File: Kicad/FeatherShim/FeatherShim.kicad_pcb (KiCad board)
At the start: 2 copper layers, 51 x 33 mm, 3 parts, among them P1 Feather, P2 CONN_01X16, P3 CONN_01X12

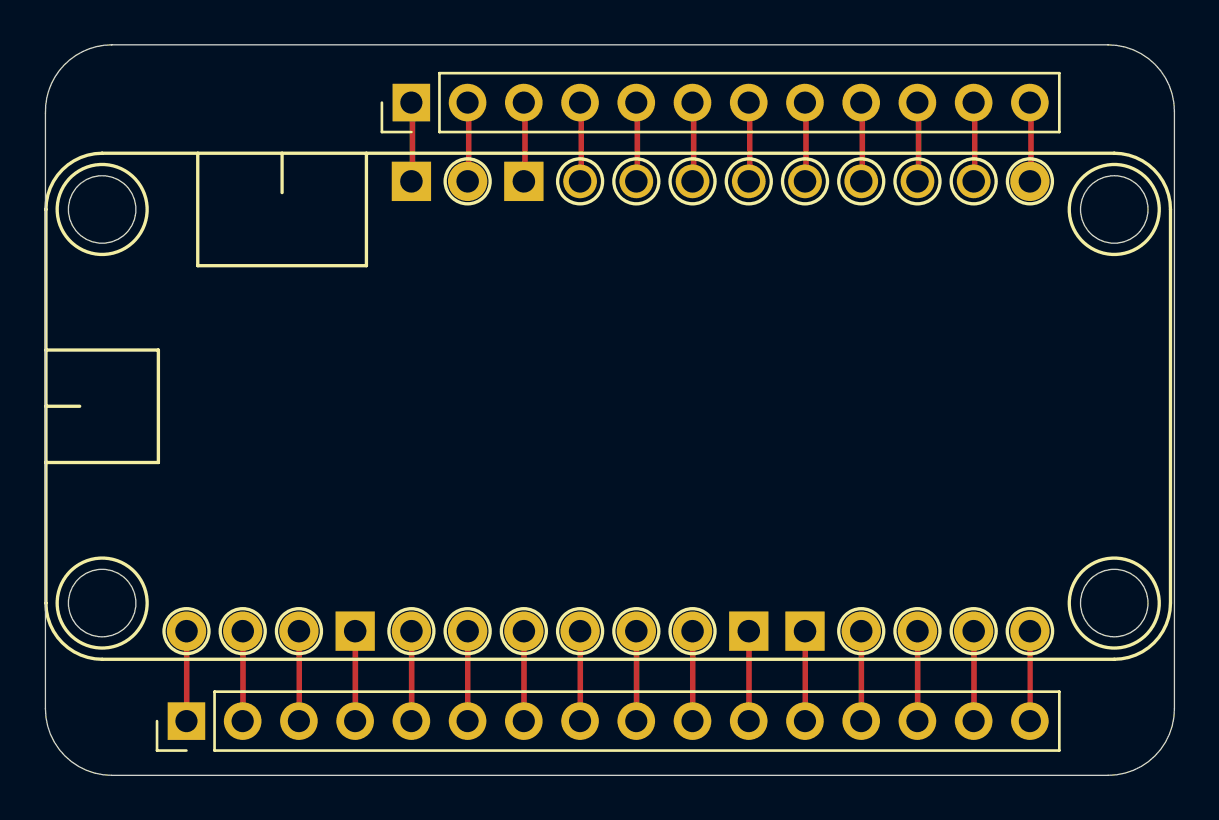
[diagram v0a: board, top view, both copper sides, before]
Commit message: thicken power traces
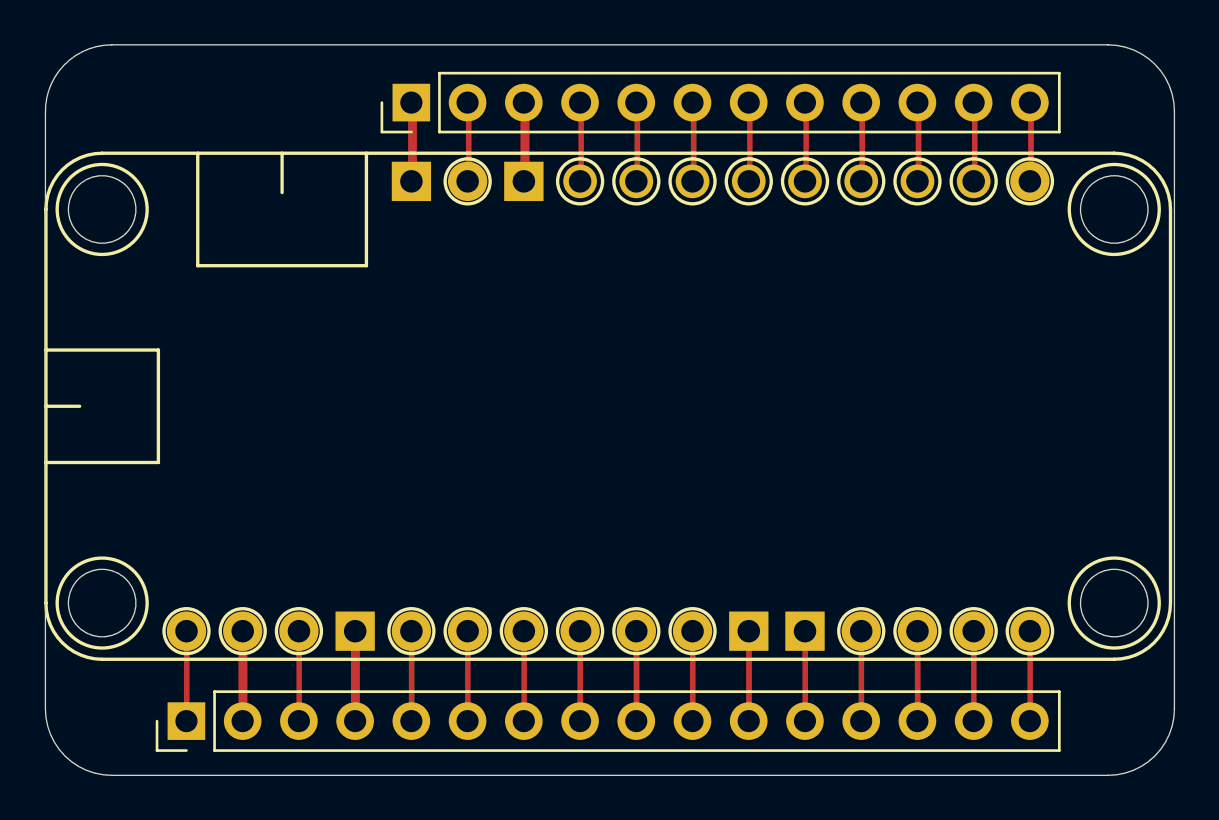
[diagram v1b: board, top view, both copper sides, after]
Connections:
- net Net-(P1-Pad2) renamed /3V3
- net Net-(P1-Pad26) renamed VBUS
- net Net-(P1-Pad28) renamed +BATT
- net Net-(P1-Pad4) renamed GND
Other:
- net class Power added: clearance 0.2, trace_width 0.4, via_dia 0.8, via_drill 0.4
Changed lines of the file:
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@@
   (net 20 "Net-(P1-Pad5)")
   (net 21 "Net-(P1-Pad3)")
-  (net 22 "Net-(P1-Pad2)")
-  (net 23 "Net-(P1-Pad1)")
-  (net 24 "Net-(P1-Pad12)")
-  (net 25 "Net-(P1-Pad11)")
-  (net 26 "Net-(P1-Pad26)")
-  (net 27 "Net-(P1-Pad4)")
-  (net 28 "Net-(P1-Pad28)")
+  (net 22 "Net-(P1-Pad1)")
+  (net 23 "Net-(P1-Pad12)")
+  (net 24 "Net-(P1-Pad11)")
+  (net 25 /3V3)
+  (net 26 VBUS)
+  (net 27 +BATT)
+  (net 28 GND)
   (net_class Default "This is the default net class."
     (clearance 0.2)
@@
     (add_net "Net-(P1-Pad18)")
     (add_net "Net-(P1-Pad19)")
-    (add_net "Net-(P1-Pad2)")
     (add_net "Net-(P1-Pad20)")
     (add_net "Net-(P1-Pad21)")
@@
     (add_net "Net-(P1-Pad24)")
     (add_net "Net-(P1-Pad25)")
-    (add_net "Net-(P1-Pad26)")
     (add_net "Net-(P1-Pad27)")
-    (add_net "Net-(P1-Pad28)")
     (add_net "Net-(P1-Pad3)")
-    (add_net "Net-(P1-Pad4)")
     (add_net "Net-(P1-Pad5)")
     (add_net "Net-(P1-Pad6)")
@@
     (add_net "Net-(P1-Pad8)")
     (add_net "Net-(P1-Pad9)")
+  )
+  (net_class Power ""
+    (clearance 0.2)
+    (trace_width 0.4)
+    (via_dia 0.8)
+    (via_drill 0.4)
+    (uvia_dia 0.3)
+    (uvia_drill 0.1)
+    (add_net +BATT)
+    (add_net /3V3)
+    (add_net GND)
+    (add_net VBUS)
   )
   (module FeatherShimLibs:Pin_Header_Straight_1x16_Pitch2.54mm (layer F.Cu)
@@
     )
     (pad 1 thru_hole rect (at 0 0 90) (size 1.7 1.7) (drill 1) (layers *.Cu *.Mask)
-      (net 23 "Net-(P1-Pad1)"))
+      (net 22 "Net-(P1-Pad1)"))
     (pad 2 thru_hole oval (at 0 2.54 90) (size 1.7 1.7) (drill 1) (layers *.Cu *.Mask)
-      (net 22 "Net-(P1-Pad2)"))
+      (net 25 /3V3))
     (pad 3 thru_hole oval (at 0 5.08 90) (size 1.7 1.7) (drill 1) (layers *.Cu *.Mask)
       (net 21 "Net-(P1-Pad3)"))
     (pad 4 thru_hole oval (at 0 7.62 90) (size 1.7 1.7) (drill 1) (layers *.Cu *.Mask)
-      (net 27 "Net-(P1-Pad4)"))
+      (net 28 GND))
     (pad 5 thru_hole oval (at 0 10.16 90) (size 1.7 1.7) (drill 1) (layers *.Cu *.Mask)
       (net 20 "Net-(P1-Pad5)"))
@@
       (net 15 "Net-(P1-Pad10)"))
     (pad 11 thru_hole oval (at 0 25.4 90) (size 1.7 1.7) (drill 1) (layers *.Cu *.Mask)
-      (net 25 "Net-(P1-Pad11)"))
+      (net 24 "Net-(P1-Pad11)"))
     (pad 12 thru_hole oval (at 0 27.94 90) (size 1.7 1.7) (drill 1) (layers *.Cu *.Mask)
-      (net 24 "Net-(P1-Pad12)"))
+      (net 23 "Net-(P1-Pad12)"))
     (pad 13 thru_hole oval (at 0 30.48 90) (size 1.7 1.7) (drill 1) (layers *.Cu *.Mask)
       (net 14 "Net-(P1-Pad13)"))
@@
     )
     (pad 1 thru_hole rect (at 0 0 90) (size 1.7 1.7) (drill 1) (layers *.Cu *.Mask)
-      (net 28 "Net-(P1-Pad28)"))
+      (net 27 +BATT))
     (pad 2 thru_hole oval (at 0 2.54 90) (size 1.7 1.7) (drill 1) (layers *.Cu *.Mask)
       (net 1 "Net-(P1-Pad27)"))
     (pad 3 thru_hole oval (at 0 5.08 90) (size 1.7 1.7) (drill 1) (layers *.Cu *.Mask)
-      (net 26 "Net-(P1-Pad26)"))
+      (net 26 VBUS))
     (pad 4 thru_hole oval (at 0 7.62 90) (size 1.7 1.7) (drill 1) (layers *.Cu *.Mask)
       (net 2 "Net-(P1-Pad25)"))
@@
       (net 21 "Net-(P1-Pad3)"))
     (pad 2 thru_hole circle (at -16.51 10.16) (size 1.778 1.778) (drill 1.016) (layers *.Cu *.Mask)
-      (net 22 "Net-(P1-Pad2)"))
+      (net 25 /3V3))
     (pad 1 thru_hole circle (at -19.05 10.16) (size 1.778 1.778) (drill 1.016) (layers *.Cu *.Mask)
-      (net 23 "Net-(P1-Pad1)"))
+      (net 22 "Net-(P1-Pad1)"))
     (pad 12 thru_hole rect (at 8.89 10.16) (size 1.778 1.778) (drill 1.016) (layers *.Cu *.Mask)
-      (net 24 "Net-(P1-Pad12)"))
+      (net 23 "Net-(P1-Pad12)"))
     (pad 11 thru_hole rect (at 6.35 10.16) (size 1.778 1.778) (drill 1.016) (layers *.Cu *.Mask)
-      (net 25 "Net-(P1-Pad11)"))
+      (net 24 "Net-(P1-Pad11)"))
     (pad 26 thru_hole rect (at -3.81 -10.16) (size 1.778 1.778) (drill 1.016) (layers *.Cu *.Mask)
-      (net 26 "Net-(P1-Pad26)"))
+      (net 26 VBUS))
     (pad 28 thru_hole rect (at -8.89 -10.16) (size 1.778 1.778) (drill 1.016) (layers *.Cu *.Mask)
-      (net 28 "Net-(P1-Pad28)"))
+      (net 27 +BATT))
     (pad 4 thru_hole rect (at -11.43 10.16) (size 1.778 1.778) (drill 1.016) (layers *.Cu *.Mask)
-      (net 27 "Net-(P1-Pad4)"))
+      (net 28 GND))
     (model M0.wrl
       (at (xyz 0 0 0))
@@
   (segment (start 141.461501 117.523401) (end 141.4881 117.55) (width 0.25) (layer F.Cu) (net 21))
   (segment (start 141.461501 113.74) (end 141.461501 117.523401) (width 0.25) (layer F.Cu) (net 21))
-  (segment (start 138.921501 117.523401) (end 138.9481 117.55) (width 0.25) (layer F.Cu) (net 22))
-  (segment (start 138.921501 113.74) (end 138.921501 117.523401) (width 0.25) (layer F.Cu) (net 22))
-  (segment (start 136.381501 117.523401) (end 136.4081 117.55) (width 0.25) (layer F.Cu) (net 23))
-  (segment (start 136.381501 113.74) (end 136.381501 117.523401) (width 0.25) (layer F.Cu) (net 23))
-  (segment (start 164.321501 117.523401) (end 164.3481 117.55) (width 0.25) (layer F.Cu) (net 24))
-  (segment (start 164.321501 113.74) (end 164.321501 117.523401) (width 0.25) (layer F.Cu) (net 24))
-  (segment (start 161.781501 117.523401) (end 161.8081 117.55) (width 0.25) (layer F.Cu) (net 25))
-  (segment (start 161.781501 113.74) (end 161.781501 117.523401) (width 0.25) (layer F.Cu) (net 25))
-  (segment (start 151.6608 93.380701) (end 151.621501 93.42) (width 0.25) (layer F.Cu) (net 26))
-  (segment (start 151.6608 89.61) (end 151.6608 93.380701) (width 0.25) (layer F.Cu) (net 26))
-  (segment (start 144.001501 117.523401) (end 144.0281 117.55) (width 0.25) (layer F.Cu) (net 27))
-  (segment (start 144.001501 113.74) (end 144.001501 117.523401) (width 0.25) (layer F.Cu) (net 27))
-  (segment (start 146.5808 93.380701) (end 146.541501 93.42) (width 0.25) (layer F.Cu) (net 28))
-  (segment (start 146.5808 89.61) (end 146.5808 93.380701) (width 0.25) (layer F.Cu) (net 28))
+  (segment (start 138.921501 117.523401) (end 138.9481 117.55) (width 0.4) (layer F.Cu) (net 25))
+  (segment (start 138.921501 113.74) (end 138.921501 117.523401) (width 0.4) (layer F.Cu) (net 25))
+  (segment (start 136.381501 117.523401) (end 136.4081 117.55) (width 0.25) (layer F.Cu) (net 22))
+  (segment (start 136.381501 113.74) (end 136.381501 117.523401) (width 0.25) (layer F.Cu) (net 22))
+  (segment (start 164.321501 117.523401) (end 164.3481 117.55) (width 0.25) (layer F.Cu) (net 23))
+  (segment (start 164.321501 113.74) (end 164.321501 117.523401) (width 0.25) (layer F.Cu) (net 23))
+  (segment (start 161.781501 117.523401) (end 161.8081 117.55) (width 0.25) (layer F.Cu) (net 24))
+  (segment (start 161.781501 113.74) (end 161.781501 117.523401) (width 0.25) (layer F.Cu) (net 24))
+  (segment (start 151.6608 93.380701) (end 151.621501 93.42) (width 0.4) (layer F.Cu) (net 26))
+  (segment (start 151.6608 89.61) (end 151.6608 93.380701) (width 0.4) (layer F.Cu) (net 26))
+  (segment (start 144.001501 117.523401) (end 144.0281 117.55) (width 0.4) (layer F.Cu) (net 28))
+  (segment (start 144.001501 113.74) (end 144.001501 117.523401) (width 0.4) (layer F.Cu) (net 28))
+  (segment (start 146.5808 93.380701) (end 146.541501 93.42) (width 0.4) (layer F.Cu) (net 27))
+  (segment (start 146.5808 89.61) (end 146.5808 93.380701) (width 0.4) (layer F.Cu) (net 27))
 )
